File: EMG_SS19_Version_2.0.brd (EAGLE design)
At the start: 160 x 100 mm, 220 parts, among them T11 OPA388, T12 OPA388, T21 OPA388, T22 OPA388

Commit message: next Version of layout 2.0: - changed position of leds, buttons and jtag connector - not every pin is routed to a connector pin - AGND,DGND on top and bottom
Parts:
- removed LED_ACT: (no value), led:LED3MM
- removed P1: (no value), con-lstb:MA05-1
- removed P2: (no value), con-lstb:MA08-1
- removed RESET: RESET, electricalmeter:PBTH
- added LED7: (no value), led:CHIP-LED0805
- added RESET_BTN: PUSH-BUTTONSURFACE-MOUNT, Taster:HDKJ
- BTN_1, BTN_2, BTN_3, BTN_4: value (none) -> PUSH-BUTTONSURFACE-MOUNT; device electricalmeter:PBTH -> Taster:HDKJ
- LED1, LED2, LED3, LED4, LED5, LED6: device led:LED3MM -> led:CHIP-LED0805
- moved JTAG 136.8 mm to (107.7, 94.2)
- moved JP14 111.9 mm to (122.9, 94.5)
- moved C110 111.6 mm to (106.9, 74.3), turned to 90 degrees
- moved R101 107.6 mm to (109.9, 74.2), turned to 90 degrees
- moved R2 96.6 mm to (106.3, 7.68)
- moved DGND1 91.4 mm to (114.3, 25.8)
- moved LED4 90.4 mm to (146.3, 8.38), turned to 0 degrees
- moved R110 84.2 mm to (143.3, 8.13), turned to 270 degrees
- moved LED5 82.7 mm to (146.3, 13.7), turned to 0 degrees
- moved CLOCK 80.6 mm to (156.1, 7.87), turned to 270 degrees
- moved LED6 77.2 mm to (146.6, 19.1), turned to 0 degrees
- moved R116 76.0 mm to (135.9, 8.13), turned to 270 degrees
- moved R111 75.8 mm to (143.3, 13.5), turned to 270 degrees
- moved R112 69.4 mm to (143.3, 18.8), turned to 270 degrees
- moved R115 66.6 mm to (135.9, 13.5), turned to 270 degrees
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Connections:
- removed net N$56: P2.8, U$1.42
- removed net N$78: P1.1, U$1.41
- removed net N$79: P1.2, U$1.40
- removed net N$80: P1.3, U$1.34
- removed net N$81: P1.4, U$1.36
- removed net N$82: P1.5, U$1.37
- net ACT_LED: now also LED7.C, U$1.83; no longer LED_ACT.K, U$1.87
- net BTN1: now also BTN_1.OU1, BTN_1.OUT2, U$1.87; no longer BTN_1.2, U$1.86
- net BTN2: now also BTN_2.OU1, BTN_2.OUT2, U$1.86; no longer BTN_2.2, U$1.85
- net BTN3: now also BTN_3.OU1, BTN_3.OUT2, U$1.85; no longer BTN_3.2, U$1.83
- net BTN4: now also BTN_4.OU1, BTN_4.OUT2; no longer BTN_4.2
- net DGND: now also BTN_1.IN1, BTN_1.IN2, BTN_2.IN1, BTN_2.IN2, BTN_3.IN1, BTN_3.IN2, BTN_4.IN1, BTN_4.IN2, RESET_BTN.OU1, RESET_BTN.OUT2; no longer BTN_1.1, BTN_2.1, BTN_3.1, BTN_4.1, RESET.2
- net LED1: now also LED1.C, U$1.37; no longer LED3.K, U$1.93
- net LED2: now also LED2.C, U$1.36; no longer LED2.K, U$1.91
- net LED3: now also LED3.C, U$1.34; no longer LED1.K, U$1.88
- net LED4: now also LED4.C, U$1.42; no longer LED4.K, U$1.89
- net LED5: now also LED5.C, U$1.41; no longer LED5.K, U$1.90
- net LED6: now also LED6.C, U$1.40; no longer LED6.K, U$1.92
- net N$23: now also LED1.A; no longer LED3.A
- net N$46: now also LED3.A; no longer LED1.A
- net N$47: now also LED7.A; no longer LED_ACT.A
- net N$63: no longer P2.7
- net N$64: no longer P2.6
- net N$65: no longer P2.5
- net N$66: no longer P2.4
- net N$67: no longer P2.3
- net N$68: no longer P2.2
- net N$69: no longer P2.1
- net RESET: now also RESET_BTN.IN1, RESET_BTN.IN2; no longer RESET.1
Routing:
- net DVCC: track 167.8 -> 371.3 mm, vias 4 -> 0
- net RESET: track 21.3 -> 75.4 mm, vias 1 -> 2
- net MCLK: track 9.11 -> 61.6 mm
- net SMCLK: track 11.8 -> 61.3 mm
- net RTCCLK: track 15.5 -> 64.3 mm, vias 1 -> 2
- net ACLK: track 11.5 -> 57.9 mm, vias 2 -> 0
- net TMS: track 20.9 -> 65.3 mm, vias 1 -> 0
- net TDI: track 20.9 -> 61.2 mm, vias 1 -> 0
- net TEST/SBWTCK: track 20.8 -> 58.7 mm, vias 1 -> 0
- net TDO: track 20.9 -> 55.2 mm, vias 1 -> 0
- net LED6: track 69.0 -> 35.1 mm, vias 2 -> 0
- net TCK: track 21.2 -> 54.1 mm, vias 1 -> 2
- net BTN4: track 26.9 -> 57.4 mm
- net BTN1: track 52.2 -> 24.0 mm
- net EXT: track 0.00 -> 27.8 mm
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- added copper zone on layer 1, net DGND
- added copper zone on layer 16, net DGND

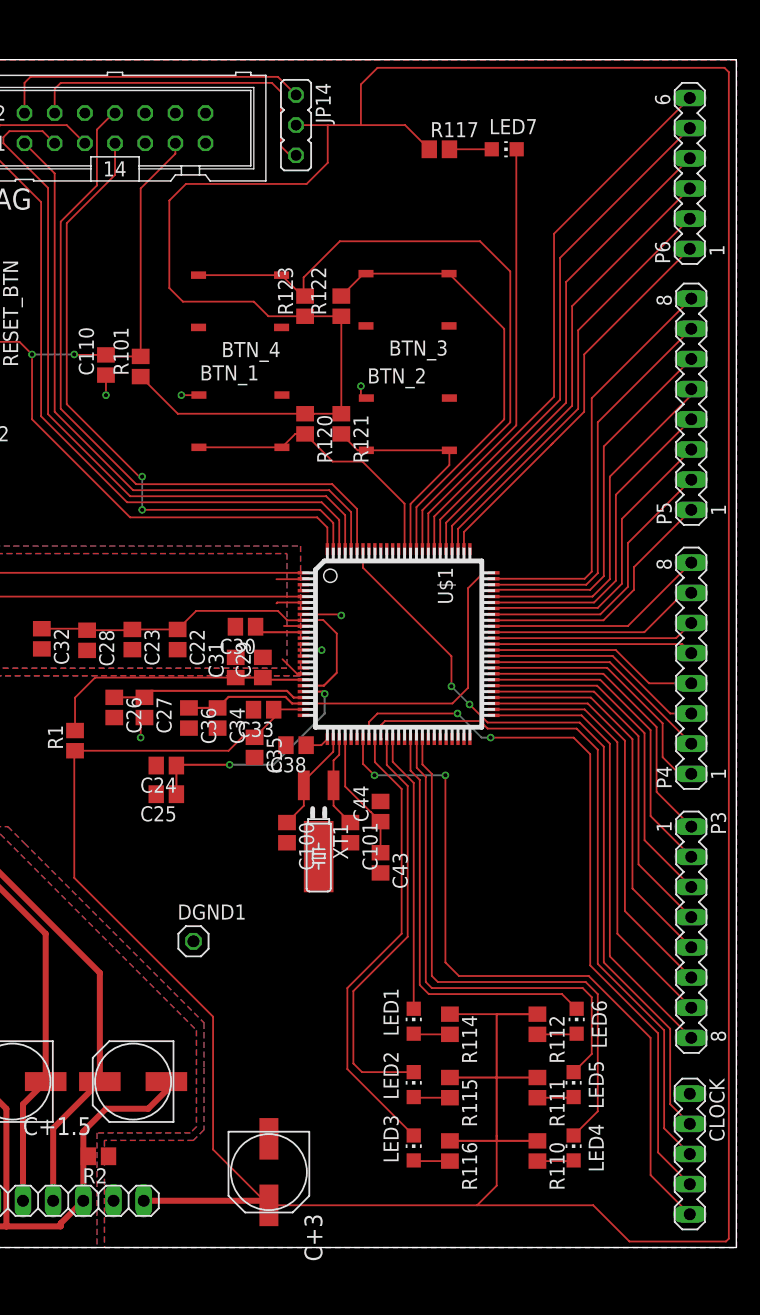
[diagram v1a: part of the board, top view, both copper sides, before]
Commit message: some improvements. - DVCC lines extended
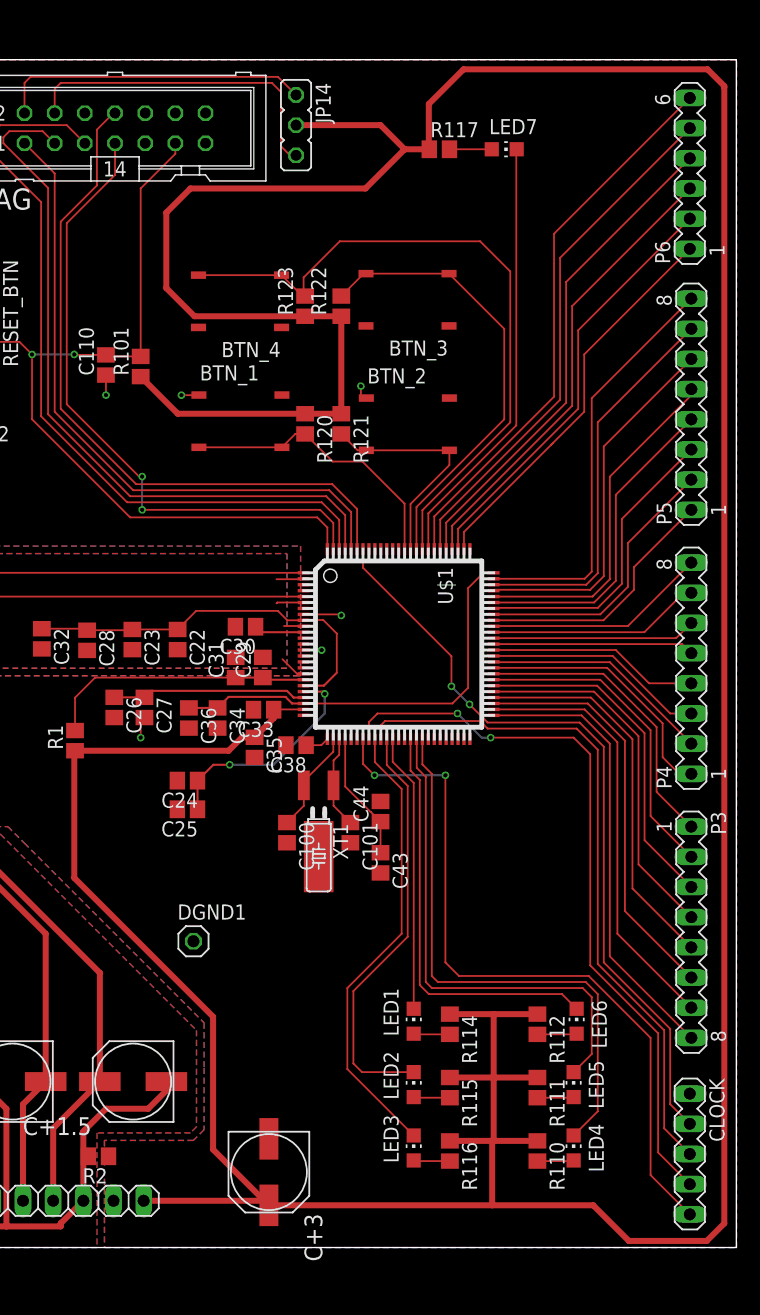
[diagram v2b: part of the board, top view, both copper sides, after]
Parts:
- moved C24 2.18 mm to (113.8, 39.3)
- moved C25 2.18 mm to (113.8, 36.9)
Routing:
- net DVCC: track 371.3 -> 367.7 mm
- net AUXVCC2: track 20.2 -> 19.0 mm
